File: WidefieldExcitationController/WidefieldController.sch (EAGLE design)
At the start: 29 parts, among them J1 5-1634503-1, J2 5-1634503-1, J3 5-1634503-1, J4 5-1634503-1

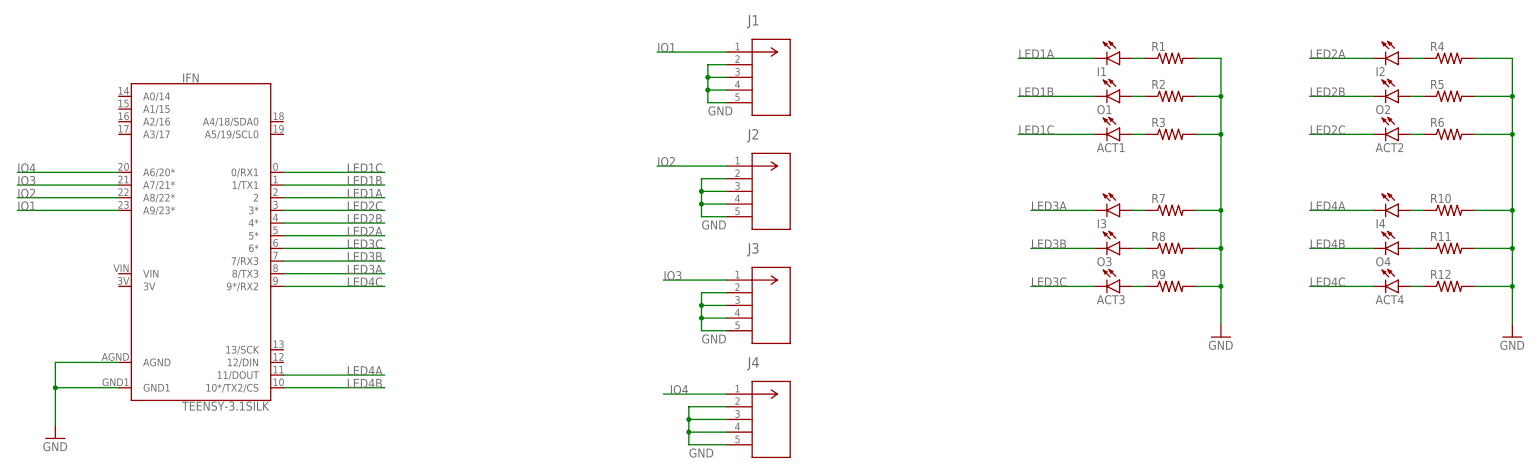
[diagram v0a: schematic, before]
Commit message: Updated WidefieldController board to be smaller
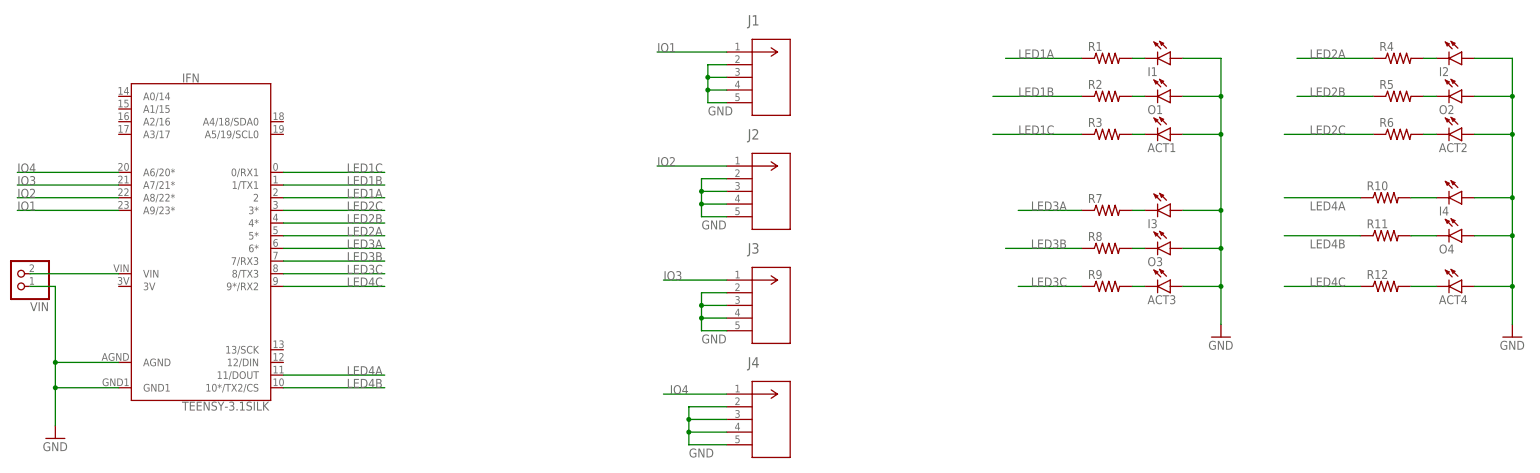
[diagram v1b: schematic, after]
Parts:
- added VIN: (no value), pinhead:PINHD-1X2
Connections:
- new net N$13: ACT1.C, R3.2
- net GND: now also ACT1.A, ACT2.A, ACT3.A, ACT4.A, I1.A, I2.A, I3.A, I4.A, O1.A, O2.A, O3.A, O4.A, VIN.1; no longer R1.2, R10.2, R11.2, R12.2, R2.2, R3.2, R4.2, R5.2, R6.2, R7.2, R8.2, R9.2
- net LED1A: now also R1.1; no longer I1.C
- net LED1B: now also R2.1; no longer O1.C
- net LED1C: now also R3.1; no longer ACT1.C
- net LED2A: now also R4.1; no longer I2.C
- net LED2B: now also R5.1; no longer O2.C
- net LED2C: now also R6.1; no longer ACT2.C
- net LED3A: now also IFN.6*, R7.1; no longer I3.C, IFN.8/TX3
- net LED3B: now also R8.1; no longer O3.C
- net LED3C: now also IFN.8/TX3, R9.1; no longer ACT3.C, IFN.6*
- net LED4A: now also R10.1; no longer I4.C
- net LED4B: now also R11.1; no longer O4.C
- net LED4C: now also R12.1; no longer ACT4.C
- net N$1: now also I2.C, R4.2; no longer I1.A, R1.1
- net N$10: now also I3.C, R7.2; no longer I4.A, R10.1
- net N$11: now also I1.C, R1.2; no longer O4.A, R11.1
- net N$12: now also O1.C, R2.2; no longer ACT4.A, R12.1
- net N$2: now also O2.C, R5.2; no longer O1.A, R2.1
- net N$3: now also ACT2.C, R6.2; no longer ACT1.A, R3.1
- net N$4: now also I4.C, R10.2; no longer I2.A, R4.1
- net N$5: now also O4.C, R11.2; no longer O2.A, R5.1
- net N$6: now also ACT4.C, R12.2; no longer ACT2.A, R6.1
- net N$7: now also IFN.VIN, VIN.2; no longer I3.A, R7.1
- net N$8: now also ACT3.C, R9.2; no longer O3.A, R8.1
- net N$9: now also O3.C, R8.2; no longer ACT3.A, R9.1
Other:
- moved on the sheet: ACT1, ACT2, ACT3, ACT4, I1, I2, I3, I4, O1, O2, O3, O4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
